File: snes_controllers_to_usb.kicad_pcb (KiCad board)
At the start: 2 copper layers, 100 x 100 mm, 31 parts, among them J1 SNES_controller_port, J2 SNES_controller_port, J3 SNES_controller_port, J4 SNES_controller_port, Q1 BSS123, Q2 BSS123, Q3 BSS123, Q4 BSS123, SW1 RST_PUSH, U1 PicoW

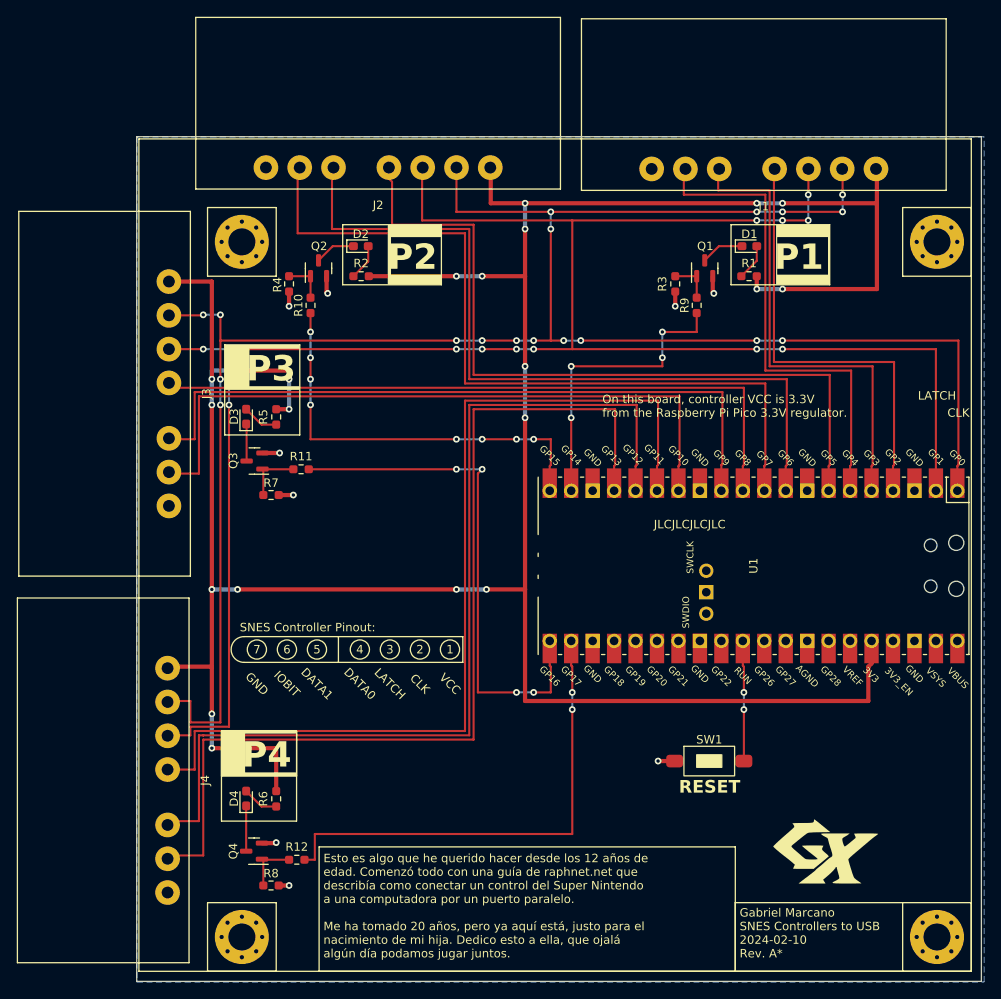
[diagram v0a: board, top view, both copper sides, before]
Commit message: Update to KiCAD 8, revision B, move some resistors
 - Update schematic and PCB to KiCAD8
 - Move R7, R8, R9, and R10 so they no longer make a voltage divider at
   the transistor bases
 - Updated drawings
 - Replaced SNES port footprint with one where the silkscreen doesn't go
   past the end of the board
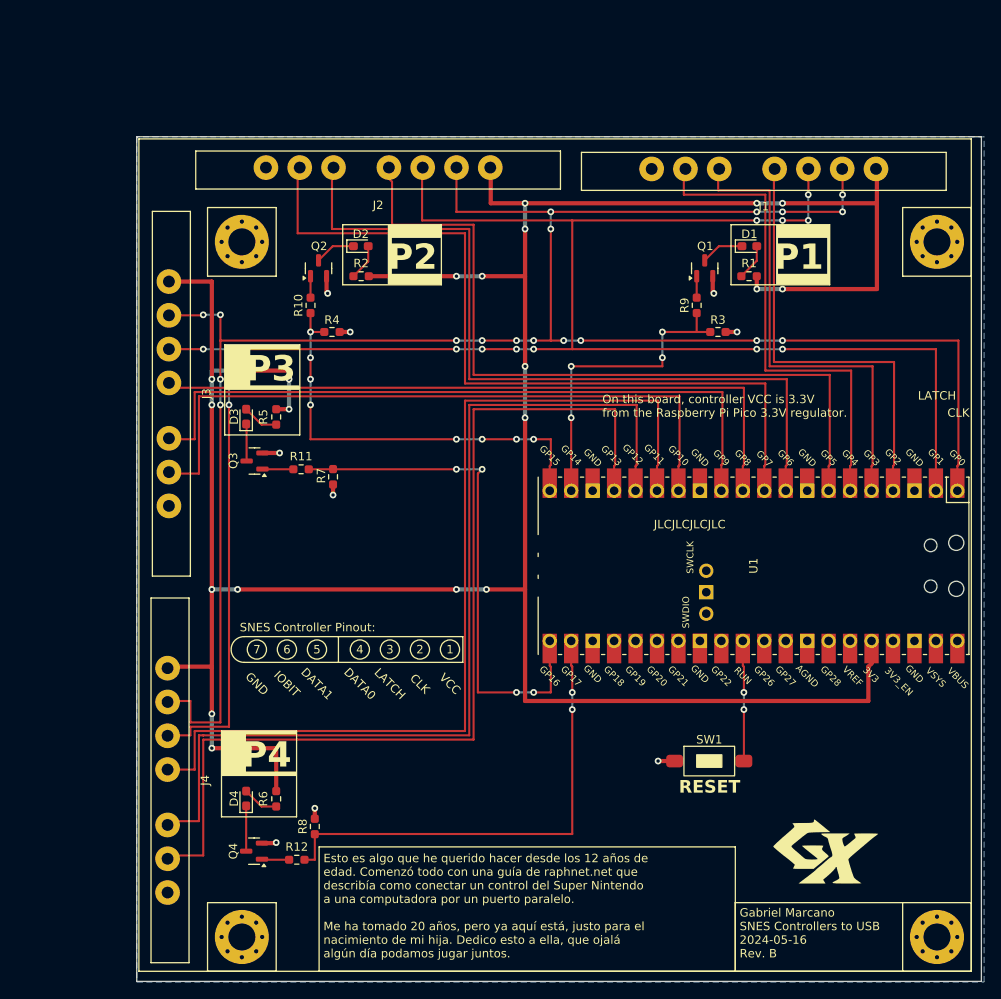
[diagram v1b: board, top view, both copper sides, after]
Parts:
- J1, J2, J3, J4: footprint Marcano:SNES_CONTROLLER_PORT_FEMALE -> Marcano:SNES_CONTROLLER_PORT_FEMALE_SHORT
- moved R8 8.70 mm to (103.6, 138.8), turned to 90 degrees
- moved R7 7.65 mm to (105.8, 97.4), turned to -90 degrees
- moved R4 7.63 mm to (105.7, 80.3), turned to 0 degrees
- moved R3 7.61 mm to (151.4, 80.3), turned to 0 degrees
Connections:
- R3 pad 1: Net-(Q1-G) -> /C0_CONN
- R4 pad 1: Net-(Q2-G) -> /C1_CONN
- R7 pad 1: Net-(Q3-G) -> /C2_CONN
- R8 pad 1: Net-(Q4-G) -> /C3_CONN
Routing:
- net Net-(Q4-G): track 6.10 -> 3.14 mm
- net Net-(Q2-G): track 5.22 -> 2.54 mm
- net Net-(Q3-G): track 6.20 -> 3.63 mm
- net Net-(Q1-G): track 5.08 -> 2.54 mm
- net /C1_CONN: track 49.5 -> 51.2 mm
- net /C0_CONN: track 35.9 -> 37.5 mm
- net GND: track 16.2 -> 15.0 mm
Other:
- board text added: "Gabriel Marcano SNES Controllers to USB ${ISSUE_DATE} Rev. ${REVISION}"
- board text removed: "Gabriel Marcano SNES Controllers to USB 2024-02-10 Rev. A*"
